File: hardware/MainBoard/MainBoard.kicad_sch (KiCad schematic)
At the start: 27 parts, among them J1 Therm., J2 SSR, J3 Serial, J4 5Vin, J5 SSR, J7 SSR, J8 SSR, SW1 Boot Mode, SW2 RESET, U1 ESP-12F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

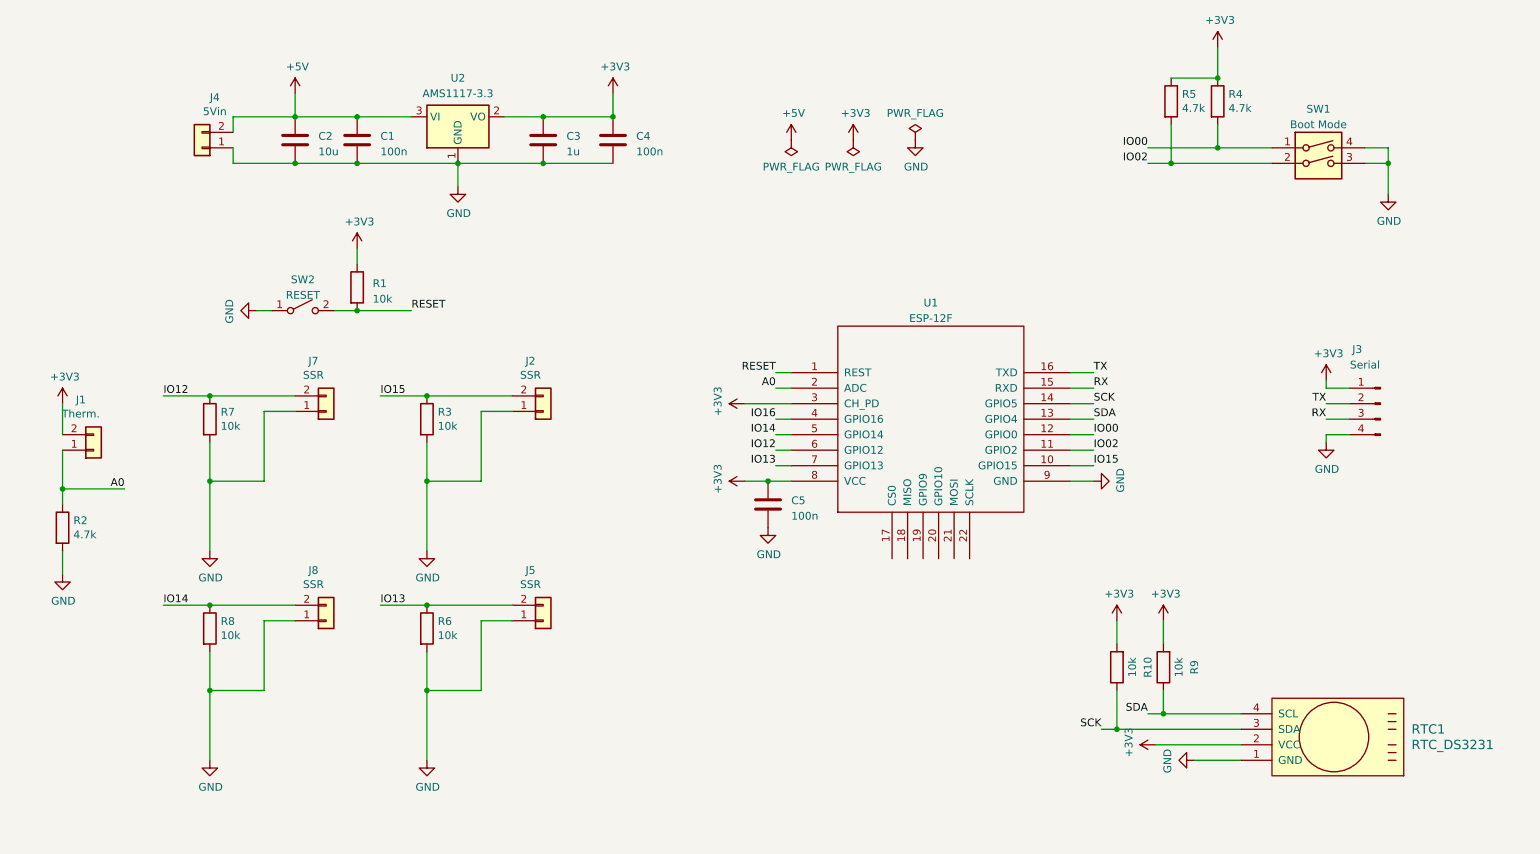
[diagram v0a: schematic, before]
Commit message: led indicators added to outputs
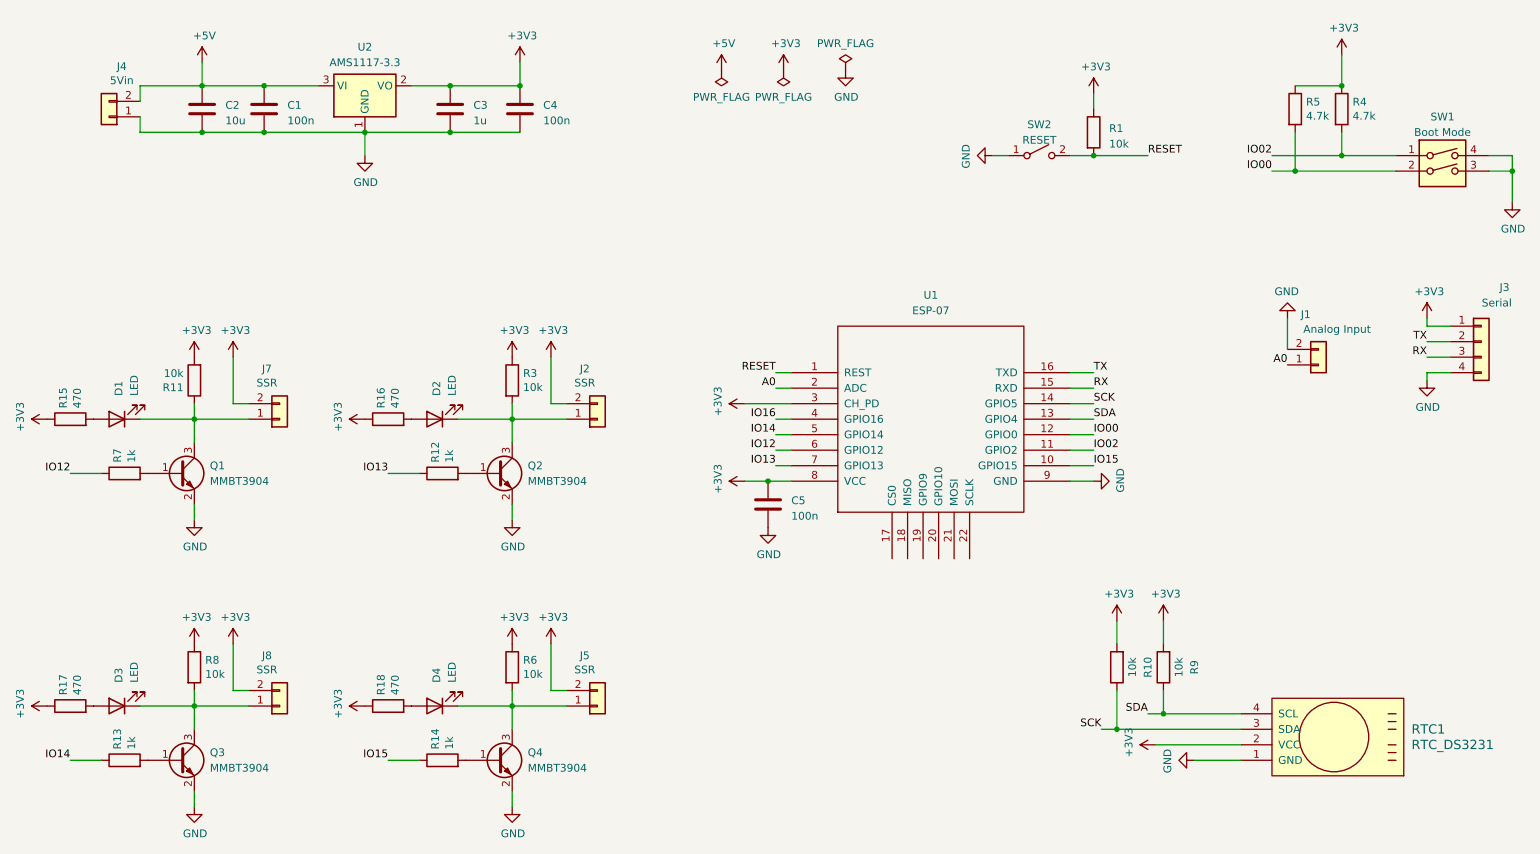
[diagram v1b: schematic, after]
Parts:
- removed R2: 4.7k, Resistor_SMD:R_1206_3216Metric_Pad1.30x1.75mm_HandSolder, symbol Device:R
- added D1, D2, D3, D4: LED, LED_SMD:LED_1206_3216Metric_Pad1.42x1.75mm_HandSolder, symbol Device:LED
- added Q1, Q2, Q3, Q4: MMBT3904, Package_TO_SOT_SMD:SOT-23, symbol Transistor_BJT:MMBT3904
- added R11: 10k, Resistor_SMD:R_1206_3216Metric_Pad1.30x1.75mm_HandSolder, symbol Device:R
- added R12, R13, R14: 1k, Resistor_SMD:R_1206_3216Metric_Pad1.30x1.75mm_HandSolder, symbol Device:R
- added R15, R16, R17, R18: 470, Resistor_SMD:R_1206_3216Metric_Pad1.30x1.75mm_HandSolder, symbol Device:R
- J1: value Therm. -> Analog Input
- J3: footprint Connector_PinHeader_2.54mm:PinHeader_1x04_P2.54mm_Vertical -> Connector_JST:JST_XH_B4B-XH-A_1x04_P2.50mm_Vertical; symbol Connector:Conn_01x04_Pin -> Connector_Generic:Conn_01x04
- R7: value 10k -> 1k
- U1: value ESP-12F -> ESP-07
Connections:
- net +3V3: now also J2.2 (Pin_2), J5.2 (Pin_2), J7.2 (Pin_2), J8.2 (Pin_2), R3.1, R6.1, R8.1, R11.2, R15.1, R16.1, R17.1, R18.1; no longer J1.2 (Pin_2)
- net GND: now also J1.2 (Pin_2), Q1.2 (E), Q2.2 (E), Q3.2 (E), Q4.2 (E); no longer J2.1 (Pin_1), J5.1 (Pin_1), J7.1 (Pin_1), J8.1 (Pin_1), R3.2, R6.2, R7.2, R8.2
- net IO00: now also R5.2, SW1.2; no longer R4.2, SW1.1
- net IO02: now also R4.2, SW1.1; no longer R5.2, SW1.2
- net IO12: no longer J7.2 (Pin_2)
- net IO13: now also R12.1; no longer J5.2 (Pin_2), R6.1
- net IO14: now also R13.1; no longer J8.2 (Pin_2), R8.1
- net IO15: now also R14.1; no longer J2.2 (Pin_2), R3.1
- new net: D2.1 (K), J2.1 (Pin_1), Q2.3 (C), R3.2
- new net: D3.1 (K), J8.1 (Pin_1), Q3.3 (C), R8.2
- new net: D1.1 (K), J7.1 (Pin_1), Q1.3 (C), R11.1
- new net: Q3.1 (B), R13.2
- new net: Q2.1 (B), R12.2
- new net: Q1.1 (B), R7.2
- new net: D4.2 (A), R18.2
- new net: D3.2 (A), R17.2
- new net: D2.2 (A), R16.2
- new net: D1.2 (A), R15.2
- new net: Q4.1 (B), R14.2
- new net: D4.1 (K), J5.1 (Pin_1), Q4.3 (C), R6.2
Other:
- moved on the sheet: C1, C2, C3, C4, J1, J2, J4, J5, J7, J8, R1, R3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

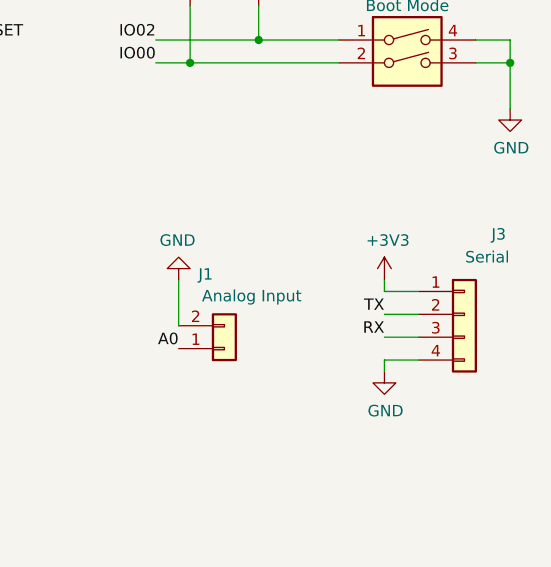
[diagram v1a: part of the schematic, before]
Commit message: gsm board module designed
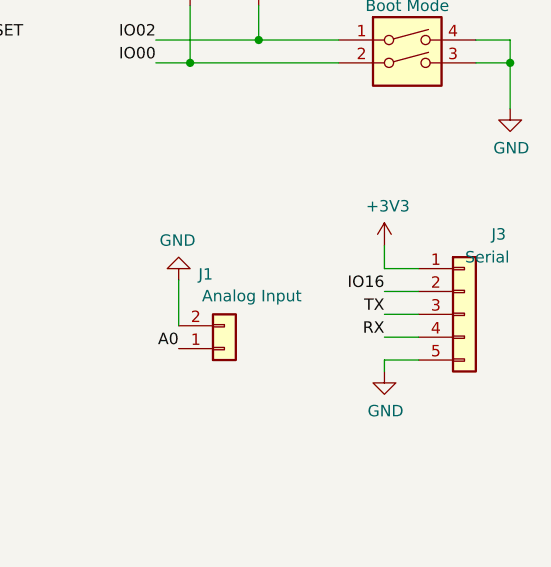
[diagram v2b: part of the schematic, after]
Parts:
- J3: footprint Connector_JST:JST_XH_B4B-XH-A_1x04_P2.50mm_Vertical -> Connector_JST:JST_XH_B5B-XH-A_1x05_P2.50mm_Vertical; symbol Connector_Generic:Conn_01x04 -> Connector_Generic:Conn_01x05
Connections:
- net GND: now also J3.5 (Pin_5); no longer J3.4 (Pin_4)
- net IO16: now also J3.2 (Pin_2)
- net RX: now also J3.4 (Pin_4); no longer J3.3 (Pin_3)
- net TX: now also J3.3 (Pin_3); no longer J3.2 (Pin_2)
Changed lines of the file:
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@@
 	(wire
 		(pts
+			(xy 254 69.85) (xy 250.19 69.85)
+		)
+		(stroke
+			(width 0)
+			(type default)
+		)
+	)
+	(wire
+		(pts
 			(xy 48.26 132.08) (xy 48.26 134.62)
 		)
@@
 	(wire
 		(pts
-			(xy 250.19 72.39) (xy 250.19 71.12)
-		)
-		(stroke
-			(width 0)
-			(type default)
-		)
-	)
-	(wire
-		(pts
 			(xy 264.16 44.45) (xy 264.16 46.99)
 		)
@@
 	(wire
 		(pts
+			(xy 250.19 69.85) (xy 250.19 67.31)
+		)
+		(stroke
+			(width 0)
+			(type default)
+		)
+	)
+	(wire
+		(pts
 			(xy 90.17 40.64) (xy 101.6 40.64)
 		)
@@
 		)
 	)
+	(label "IO16"
+		(at 250.19 72.39 180)
+		(fields_autoplaced yes)
+		(effects
+			(font
+				(size 1.27 1.27)
+			)
+			(justify right bottom)
+		)
+	)
 	(label "IO15"
 		(at 80.01 143.51 180)
@@
 	)
 	(symbol
+		(lib_id "power:+3V3")
+		(at 250.19 67.31 0)
+		(unit 1)
+		(exclude_from_sim no)
+		(in_bom yes)
+		(on_board yes)
+		(dnp no)
+		(property "Reference" "#PWR05"
+			(at 250.19 71.12 0)
+			(effects
+				(font
+					(size 1.27 1.27)
+				)
+				(hide yes)
+			)
+		)
+		(property "Value" "+3V3"
+			(at 250.571 62.9158 0)
+			(effects
+				(font
+					(size 1.27 1.27)
+				)
+			)
+		)
+		(property "Footprint" ""
+			(at 250.19 67.31 0)
+			(effects
+				(font
+					(size 1.27 1.27)
+				)
+				(hide yes)
+			)
+		)
+		(property "Datasheet" ""
+			(at 250.19 67.31 0)
+			(effects
+				(font
+					(size 1.27 1.27)
+				)
+				(hide yes)
+			)
+		)
+		(property "Description" ""
+			(at 250.19 67.31 0)
+			(effects
+				(font
+					(size 1.27 1.27)
+				)
+				(hide yes)
+			)
+		)
+		(pin "1"
+		)
+		(instances
+			(project "MainBoard"
+				(path "/aa3dbaea-63c2-4583-a05b-c2086b245f5c"
+					(reference "#PWR05")
+					(unit 1)
+				)
+			)
+		)
+	)
+	(symbol
 		(lib_id "Transistor_BJT:MMBT3904")
 		(at 97.79 96.52 0)
@@
 	)
 	(symbol
-		(lib_id "Connector_Generic:Conn_01x04")
+		(lib_id "Connector_Generic:Conn_01x05")
 		(at 259.08 74.93 0)
 		(unit 1)
@@
 			)
 		)
-		(property "Footprint" "Connector_JST:JST_XH_B4B-XH-A_1x04_P2.50mm_Vertical"
+		(property "Footprint" "Connector_JST:JST_XH_B5B-XH-A_1x05_P2.50mm_Vertical"
 			(at 259.08 74.93 0)
 			(effects
@@
 			)
 		)
-		(property "Description" "Generic connector, single row, 01x04, script generated (kicad-library-utils/schlib/autogen/connector/)"
+		(property "Description" "Generic connector, single row, 01x05, script generated (kicad-library-utils/schlib/autogen/connector/)"
 			(at 259.08 74.93 0)
 			(effects
@@
 		(pin "4"
 		)
+		(pin "5"
+		)
 		(instances
 			(project "MainBoard"
@@
 					(unit 1)
 				)
-			)
-		)
-	)
-	(symbol
-		(lib_id "power:+3V3")
-		(at 250.19 71.12 0)
-		(unit 1)
-		(exclude_from_sim no)
-		(in_bom yes)
-		(on_board yes)
-		(dnp no)
-		(property "Reference" "#PWR015"
-			(at 250.19 74.93 0)
-			(effects
-				(font
-					(size 1.27 1.27)
-				)
-				(hide yes)
-			)
-		)
-		(property "Value" "+3V3"
-			(at 250.571 66.7258 0)
-			(effects
-				(font
-					(size 1.27 1.27)
-				)
-			)
-		)
-		(property "Footprint" ""
-			(at 250.19 71.12 0)
-			(effects
-				(font
-					(size 1.27 1.27)
-				)
-				(hide yes)
-			)
-		)
-		(property "Datasheet" ""
-			(at 250.19 71.12 0)
-			(effects
-				(font
-					(size 1.27 1.27)
-				)
-				(hide yes)
-			)
-		)
-		(property "Description" ""
-			(at 250.19 71.12 0)
-			(effects
-				(font
-					(size 1.27 1.27)
-				)
-				(hide yes)
-			)
-		)
-		(pin "1"
-		)
-		(instances
-			(project "MainBoard"
-				(path "/aa3dbaea-63c2-4583-a05b-c2086b245f5c"
-					(reference "#PWR015")
-					(unit 1)
-				)
-			)
-			(project "hot-plate"
-				(path "/afd3dbad-e7a8-4e4c-b77c-4065a69aefa2"
-					(reference "#PWR0102")
-					(unit 1)
-				)
